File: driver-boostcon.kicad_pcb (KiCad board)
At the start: 2 copper layers, 100 x 80 mm, 62 parts, among them IC601 ATMEGA328-P, P301 On Switch, P302 Vcc, P303 PowerGND, P304 RegulatedPWR, P305 RegulatedGND, P601 Programmer, Q401 IRFH7084, Q402 BSC016N04LS, SW601 SW_PUSH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

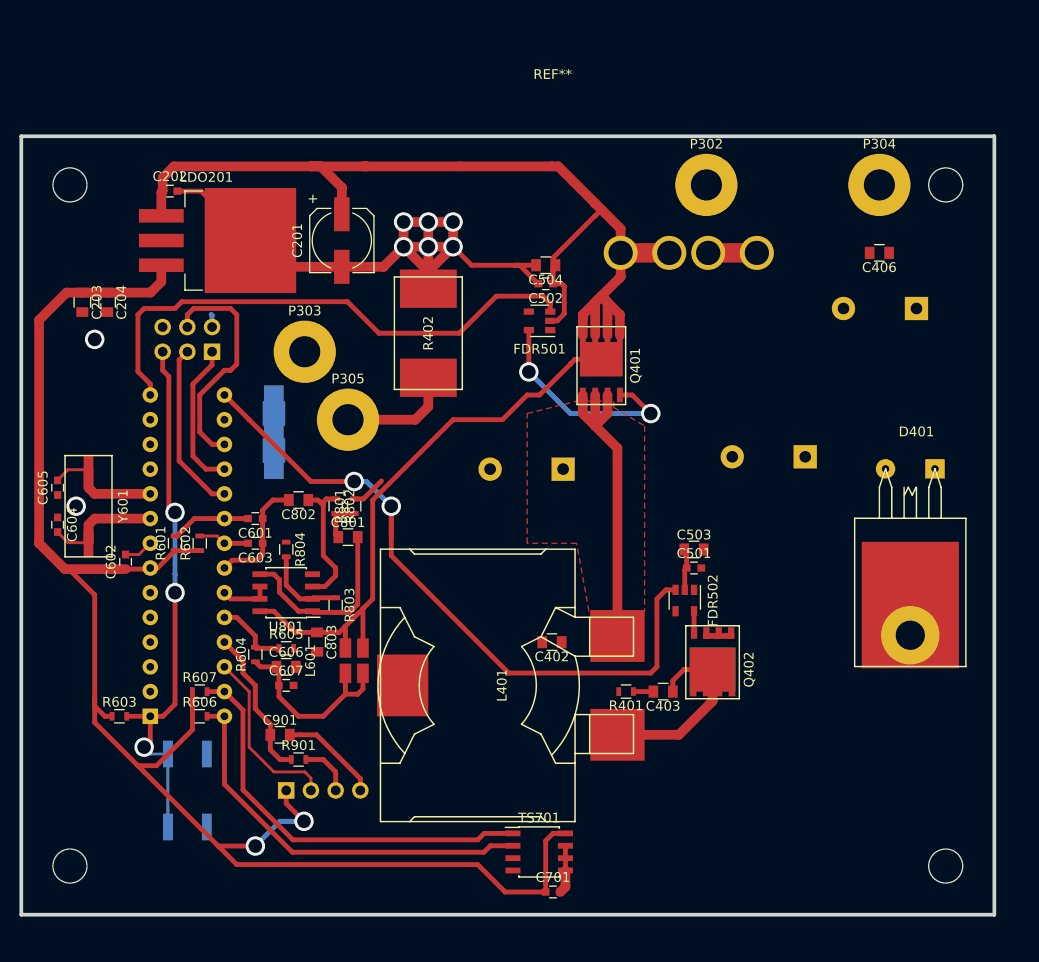
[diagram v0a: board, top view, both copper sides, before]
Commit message: Separated digital and power sections more
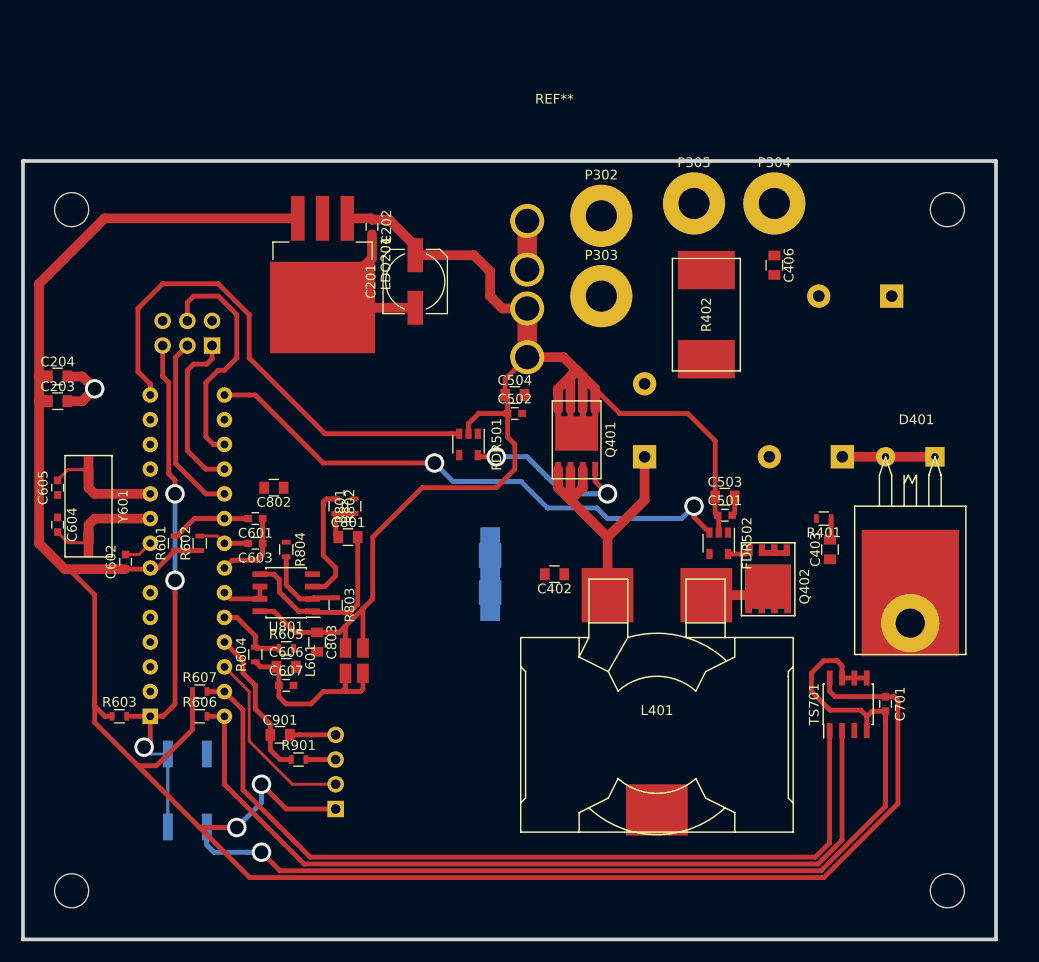
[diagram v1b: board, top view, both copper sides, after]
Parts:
- moved P305 41.9 mm to (116.8, 66.7)
- moved C701 39.3 mm to (136.5, 118.1), turned to 270 degrees
- moved TS701 35.2 mm to (132.7, 118.1), turned to 90 degrees
- moved P303 31.0 mm to (107.3, 76.2)
- moved R402 28.6 mm to (118.1, 78.1), turned to 270 degrees
- moved R401 27.0 mm to (130.2, 99.1)
- moved GND301 26.6 mm to (95.9, 104.8)
- moved C403 22.5 mm to (130.8, 102.2), turned to 90 degrees
- moved C202 21.1 mm to (83.7, 69.1), turned to 270 degrees
- moved L401 19.1 mm to (113.0, 121.3), turned to 180 degrees
- moved F301 17.0 mm to (99.7, 75.5), turned to 270 degrees
- moved FDR501 14.6 mm to (93.7, 91.4), turned to 270 degrees
- moved C502 13.7 mm to (98.4, 88.3), turned to 0 degrees
- moved C504 13.7 mm to (98.4, 86.4), turned to 0 degrees
- moved LDO201 12.2 mm to (78.7, 72.8), turned to 270 degrees
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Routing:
- net GNDD: track 8.15 -> 115.1 mm
- net +5C: track 165.1 -> 237.5 mm
- net SCL: track 42.1 -> 88.4 mm
- net GNDPWR: track 71.1 -> 25.0 mm, vias 6 -> 0
- net SDA: track 43.8 -> 89.0 mm
- net VCC: track 166.7 -> 135.3 mm
- net /CurrentSense/CurrentSignal: track 15.4 -> 0.77 mm
- net /MCU/GateDriveSignal: track 72.0 -> 57.4 mm
- net GNDREF: track 22.5 -> 12.9 mm
- net /Power stage/PowerRegulated: track 0.00 -> 9.52 mm
- net /Power stage/SwitchNode: track 20.1 -> 10.8 mm
- net /MosFET driver/PowerDriveSignal: track 22.6 -> 18.7 mm
- net /MCU/PowerDriveSignal: track 55.8 -> 52.5 mm
- net /Current Set/CurrentSetInput: track 5.49 -> 3.06 mm
- net /MCU/MISO: track 15.3 -> 17.2 mm
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- removed copper zone on F.Cu, net Net-(C401-Pad1)

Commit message: Resolved library issues
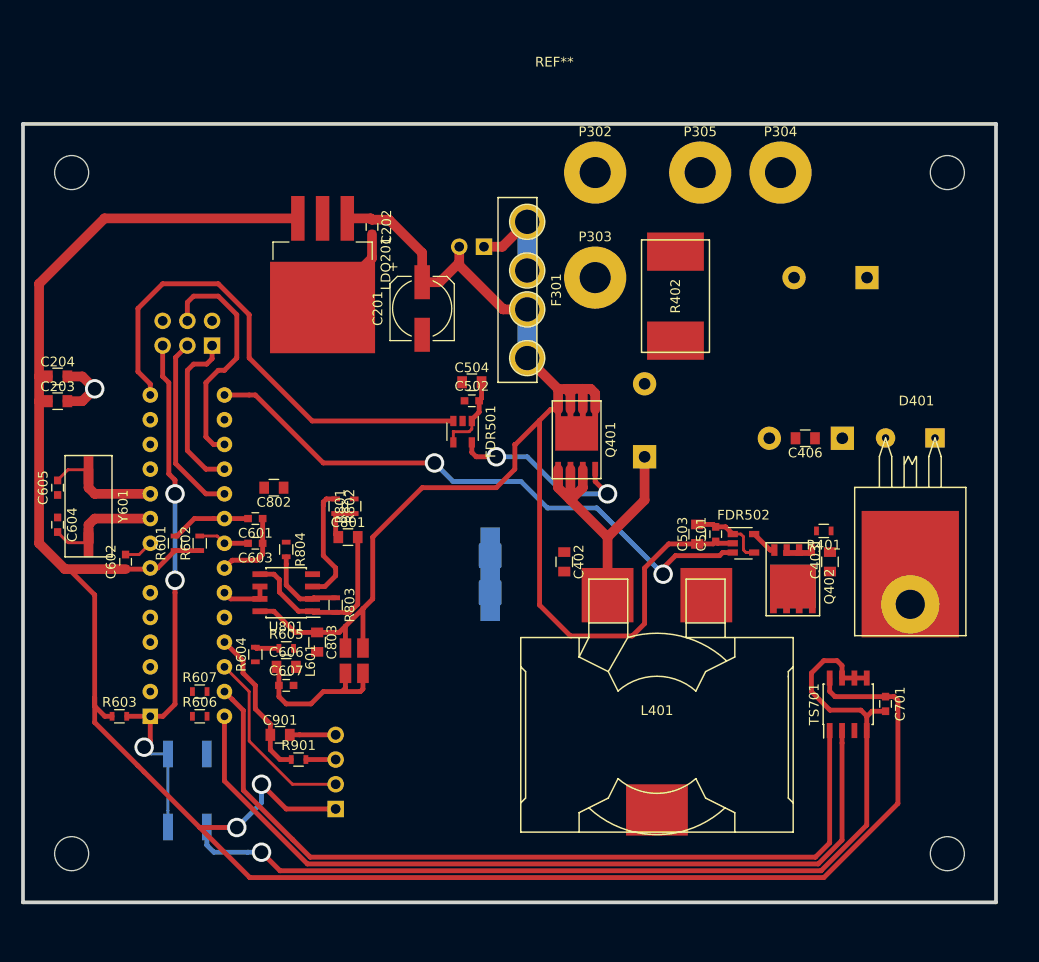
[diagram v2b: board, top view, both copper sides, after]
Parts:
- removed IC601: ATMEGA328-P, Housings_DIP:DIP-28_W7.62mm_Socket
- added J301: Fuse Bypass, Pin_Headers:Pin_Header_Angled_1x02_Pitch2.54mm, B.Cu at (95.2, 71.1)
- added U601: ATMEGA328P-PU, Housings_DIP:DIP-28_W7.62mm_Socket, B.Cu at (61.0, 119.4)
- F301: value FUSE -> Fuse; moved to F.Cu
- R604, R605: value 4.7 kOhm -> 4.7k
- R606, R607: value 4.7k -> 4.7 kOhm
- SW601: value SW_PUSH -> SW_Push
- moved C406 18.1 mm to (128.3, 90.8), turned to 180 degrees
- moved C503 4.79 mm to (117.2, 100.7), turned to 90 degrees
- moved C502 4.61 mm to (94.0, 87.0)
- moved C504 4.61 mm to (94.0, 85.1)
- moved P302 4.49 mm to (106.7, 63.5)
- moved REF** 3.81 mm to (47.9, 138.5)
- moved R402 3.70 mm to (114.9, 76.2)
- moved P304 3.24 mm to (125.7, 63.5)
- moved P305 3.24 mm to (117.5, 63.5)
- moved C405 3.17 mm to (134.6, 74.3)
- moved C201 2.87 mm to (88.9, 77.5)
- moved FDR502 2.54 mm to (121.9, 101.6), turned to 0 degrees
- moved Q402 2.54 mm to (127.0, 103.5)
- moved C501 2.16 mm to (119.1, 100.7), turned to 90 degrees
- moved P303 2.01 mm to (106.7, 74.3)
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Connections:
- F301 pad 1: Net-(F301-Pad1) -> VCC
- F301 pad 2: VCC -> Net-(F301-Pad2)
- FDR501 pad 1: (no net) -> GNDPWR
- FDR502 pad 1: (no net) -> GNDPWR
- LDO201 pad 2: (no net) -> Net-(LDO201-Pad2)
- P302 pad 1: Net-(F301-Pad1) -> Net-(F301-Pad2)
- R604 pad 1: Net-(C606-Pad1) -> +5C
- R604 pad 2: Net-(IC601-Pad24) -> SCL
- R605 pad 1: Net-(IC601-Pad24) -> +5C
- R605 pad 2: GNDREF -> SDA
- R606 pad 1: +5C -> Net-(C606-Pad1)
- R606 pad 2: SCL -> Net-(R606-Pad2)
- R607 pad 1: +5C -> Net-(R606-Pad2)
- R607 pad 2: SDA -> GNDREF
- TS701 pad 3: (no net) -> Net-(TS701-Pad3)
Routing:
- net +5C: track 237.5 -> 226.4 mm
- net /Power stage/SwitchNode: track 10.8 -> 0.00 mm
- net /Power stage/PowerRegulated: track 9.52 -> 0.00 mm
- net VCC: track 135.3 -> 143.8 mm
- net Net-(IC601-Pad24): track 7.75 -> 0.00 mm
- net Net-(F301-Pad2): track 0.00 -> 5.50 mm
- net GNDPWR: track 25.0 -> 29.9 mm
- net /MCU/GateDriveSignal: track 57.4 -> 61.2 mm
- net GNDD: track 115.1 -> 112.3 mm
- net Net-(C606-Pad1): track 18.8 -> 16.4 mm
- net Net-(C403-Pad2): track 2.22 -> 0.00 mm
- net SDA: track 89.0 -> 87.2 mm
- net /MosFET driver/PowerDriveSignal: track 18.7 -> 20.4 mm
- net /MCU/PowerDriveSignal: track 52.5 -> 51.3 mm
- net /CurrentSense/CurrentSignal: track 0.77 -> 0.00 mm
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
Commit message: Syncing
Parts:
- C202, C501, C502, C601, C602, C603, C604, C605, C607, C701: footprint Capacitors_SMD:C_0603 -> axel:C_0603_CustomText
- C203, C204, C402, C403, C406, C503, C504, C606, C801, C802, C803, C901: footprint Capacitors_SMD:C_0805 -> axel:C_0805_CustomText
- R401, R601, R602, R603, R604, R605, R606, R607, R801, R802, R803, R804, R901: footprint Resistors_SMD:R_0603 -> axel:C_0603_CustomText
- moved C203 25.8 mm to (63.5, 64.1), turned to 270 degrees
- moved C204 25.0 mm to (66.0, 64.1), turned to 270 degrees
- moved GND301 21.3 mm to (77.5, 94.0), turned to 180 degrees
- moved R605 9.94 mm to (66.0, 116.8)
- moved C802 9.44 mm to (80.6, 102.2)
- moved R607 9.03 mm to (73.0, 111.1)
- moved R604 8.54 mm to (66.0, 119.4), turned to 0 degrees
- moved R606 8.54 mm to (72.4, 113.7), turned to 90 degrees
- moved F301 6.38 mm to (100.3, 69.2)
- moved C801 5.43 mm to (83.2, 106.0), turned to 270 degrees
- moved C404 4.62 mm to (136.5, 89.5)
- moved C406 4.50 mm to (132.3, 92.7)
- moved C607 4.02 mm to (78.7, 117.5), turned to 90 degrees
- moved C201 3.86 mm to (88.3, 73.7)
- moved LDO201 3.86 mm to (78.0, 69.0)
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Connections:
- net Net-(C401-Pad1) renamed /Power stage/PowerVcc
- net Net-(C601-Pad2) renamed /MCU/AVcc
- net Net-(C603-Pad2) renamed /MCU/AREF
- net Net-(R606-Pad2) renamed /MCU/Vsense
- GND301 pad 1: GNDPWR -> GNDREF
- GND301 pad 2: GNDREF -> GNDPWR
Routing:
- net GNDREF: track 12.9 -> 113.1 mm, vias 0 -> 3
- net /CurrentSense/CurrentSignal: track 0.00 -> 94.7 mm, vias 0 -> 2
- net GNDD: track 112.3 -> 178.5 mm, vias 2 -> 5
- net GNDPWR: track 29.9 -> 74.4 mm, vias 0 -> 4
- net +5C: track 226.4 -> 257.8 mm, vias 2 -> 4
- net /Power stage/SwitchNode: track 0.00 -> 15.5 mm, vias 0 -> 3
- net /MCU/PowerDriveSignal: track 51.3 -> 59.1 mm
- net VCC: track 143.8 -> 150.3 mm
- net /MCU/Vsense: track 0.00 -> 6.32 mm
- net /MCU/MOSI: track 24.5 -> 30.1 mm
- net Net-(C801-Pad2): track 19.9 -> 14.8 mm
- net Net-(C606-Pad1): track 16.4 -> 20.5 mm
- net Net-(C801-Pad1): track 4.44 -> 7.86 mm
- net Net-(C403-Pad2): track 0.00 -> 2.22 mm
- net Net-(C802-Pad1): track 12.3 -> 10.4 mm
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- added copper zone on F.Cu, net /CurrentSense/CurrentSignal
- added copper zone on F.Cu, net /Power stage/PowerRegulated
- added copper zone on F.Cu, net /Power stage/PowerVcc
- added copper zone on B.Cu, net /Power stage/SwitchNode
- added copper zone on F.Cu, net /Power stage/SwitchNode
- added copper zone on B.Cu, net GNDD
- added copper zone on F.Cu, net GNDD
- added copper zone on B.Cu, net GNDPWR
- added copper zone on F.Cu, net GNDPWR
- added copper zone on F.Cu, net Net-(F301-Pad2)
- added copper zone on F.Cu, net VCC

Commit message: New amplifiers, fuse and general mayhem
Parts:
- removed C802: 15nF, axel:C_0805_CustomText
- removed C803: 100n, axel:C_0805_CustomText
- removed P305: RegulatedGND, Mounting_Holes:MountingHole_3.2mm_M3_Pad
- removed R801: 1.1k, axel:C_0603_CustomText
- removed R802: 1.55k, axel:C_0603_CustomText
- removed R803: 9k, axel:C_0603_CustomText
- removed R804: 1k, axel:C_0603_CustomText
- removed REF**: EuroBoard_halb_Type-I_100mmX80mm_holes, EuroBoard_Outline:EuroBoard_halb_Type-I_100mmX80mm_holes
- added R403: 0.002 Ohm, axel:R-SMD-4527, F.Cu at (123.2, 67.4)
- added R404: 0.002 Ohm, axel:R-SMD-4527, F.Cu at (123.2, 60.9)
- added R405: 0.002 Ohm, axel:R-SMD-4527, F.Cu at (123.2, 73.9)
- C801: value 3.3nF -> C_Small; footprint axel:C_0805_CustomText -> axel:C_0603_CustomText
- C901: footprint axel:C_0805_CustomText -> axel:C_0603_CustomText
- F301: footprint axel:Littlefuse-holder -> axel:Littlefuse_30mm_M5; moved to B.Cu
- Q401: value IRFH7084 -> IRF4905S; footprint axel:PQFN_5x6_Outline-B -> axel:TO-263-3Lead_NoPin2
- R401: value 5 Ohm -> 2k Ohm
- R402: value 0.002 Ohm -> 5 Ohm; footprint axel:R-SMD-4527 -> axel:C_0603_CustomText
- U801: value LM358 -> INA282
- moved U801 54.7 mm to (123.0, 80.8), turned to 0 degrees
- moved C801 45.4 mm to (123.0, 84.2), turned to 0 degrees
- moved R402 27.9 mm to (130.0, 100.0), turned to 180 degrees
- moved R401 24.9 mm to (109.8, 85.5), turned to 0 degrees
- moved C502 22.6 mm to (118.1, 89.9)
- moved C504 22.6 mm to (118.1, 88.0)
- moved FDR501 19.3 mm to (114.2, 90.0), turned to 180 degrees
- moved C402 16.6 mm to (118.0, 95.5), turned to 0 degrees
- moved P302 15.9 mm to (94.8, 53.0)
- moved P304 15.2 mm to (110.8, 61.0), turned to 270 degrees
- moved F301 11.5 mm to (94.8, 79.2)
- moved C201 10.0 mm to (83.5, 82.5), turned to 180 degrees
- moved C401 9.75 mm to (122.2, 89.0), turned to 90 degrees
- moved C405 7.90 mm to (143.0, 68.5)
- moved C404 7.76 mm to (143.0, 85.2)
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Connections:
- C404 pad 1: /Power stage/PowerRegulated -> /CurrentSense/CurrentSignal+
- C405 pad 1: /Power stage/PowerRegulated -> /CurrentSense/CurrentSignal+
- C406 pad 1: /Power stage/PowerRegulated -> /CurrentSense/CurrentSignal+
- C801 pad 1: Net-(C801-Pad1) -> GNDD
- C801 pad 2: Net-(C801-Pad2) -> +5C
- D401 pad 1: /Power stage/PowerRegulated -> /CurrentSense/CurrentSignal+
- LDO201 pad 2: Net-(LDO201-Pad2) -> (no net)
- P304 pad 1: /Power stage/PowerRegulated -> /CurrentSense/CurrentSignal-
- Q401 pad 1: /Power stage/PowerVcc -> /MosFET driver/PowerDriveSignal
- Q401 pad 3: /Power stage/PowerVcc -> VCC
- R401 pad 1: Net-(C403-Pad2) -> VCC
- R401 pad 2: GNDPWR -> /MosFET driver/PowerDriveSignal
- R402 pad 1: /CurrentSense/CurrentSignal -> Net-(C403-Pad2)
- TS701 pad 3: Net-(TS701-Pad3) -> (no net)
- U601 pad 11: Net-(U601-Pad11) -> (no net)
- U601 pad 12: Net-(U601-Pad12) -> (no net)
- U601 pad 13: Net-(U601-Pad13) -> (no net)
- U601 pad 16: Net-(U601-Pad16) -> (no net)
- U601 pad 2: Net-(U601-Pad2) -> (no net)
- U601 pad 23: /CurrentSense/CurrentSignalFiltered -> /CurrentSense/CurrentSignal
- U601 pad 3: Net-(U601-Pad3) -> (no net)
- U601 pad 4: Net-(U601-Pad4) -> (no net)
- U601 pad 5: Net-(U601-Pad5) -> (no net)
- U601 pad 6: Net-(U601-Pad6) -> (no net)
- U801 pad 1: Net-(C801-Pad2) -> /CurrentSense/CurrentSignal-
- U801 pad 2: Net-(R803-Pad1) -> GNDD
- U801 pad 3: Net-(C802-Pad1) -> GNDD
- U801 pad 4: GNDREF -> (no net)
- U801 pad 5: Net-(C801-Pad2) -> /CurrentSense/CurrentSignal
- U801 pad 6: /CurrentSense/CurrentSignalFiltered -> +5C
- U801 pad 7: /CurrentSense/CurrentSignalFiltered -> GNDD
- U801 pad 8: VCC -> /CurrentSense/CurrentSignal+
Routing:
- net VCC: track 150.3 -> 52.8 mm
- net /CurrentSense/CurrentSignal: track 94.7 -> 0.00 mm, vias 2 -> 0
- net /Power stage/PowerVcc: track 32.5 -> 0.00 mm
- net GNDPWR: track 74.4 -> 57.6 mm, vias 4 -> 1
- net GNDREF: track 113.1 -> 96.9 mm
- net Net-(C801-Pad2): track 14.8 -> 0.00 mm
- net /MosFET driver/PowerDriveSignal: track 19.1 -> 7.28 mm, vias 2 -> 0
- net GNDD: track 178.5 -> 190.2 mm
- net Net-(C802-Pad1): track 10.4 -> 0.00 mm
- net Net-(R803-Pad1): track 8.71 -> 0.00 mm
- net /Power stage/SwitchNode: track 15.5 -> 7.29 mm
- net Net-(C801-Pad1): track 7.86 -> 0.00 mm
- net Net-(F301-Pad2): track 6.02 -> 0.00 mm
- net /MCU/PowerDriveSignal: track 59.1 -> 53.1 mm
- net /CurrentSense/CurrentSignalFiltered: track 5.18 -> 0.00 mm
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- removed copper zone on F.Cu, net /CurrentSense/CurrentSignal
- removed copper zone on F.Cu, net /Power stage/PowerRegulated
- removed copper zone on F.Cu, net /Power stage/PowerVcc
- removed copper zone on F.Cu, net Net-(F301-Pad2)
- removed copper zone on F.Cu, net VCC
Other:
- board outline removed
- net class Default: trace_width 0.3 -> 0.6; via_dia 2 -> 2.5
